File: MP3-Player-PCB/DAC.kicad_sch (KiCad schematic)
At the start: 2 parts, among them J501 AudioJack3, U501 TAD5242

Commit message: Started power schematic
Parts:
- renumbered J501 to J401, U501 to U401
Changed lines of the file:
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@@
 		(dnp no)
 		(fields_autoplaced yes)
-		(property "Reference" "J501"
+		(property "Reference" "J401"
 			(at 135.255 58.42 0)
 			(effects
@@
 			(project ""
 				(path "/3f51ea9b-d2e1-4711-a47c-269e1b97e0f4/55939feb-9632-43ca-a0aa-b7cf8cf1876d"
-					(reference "J501")
+					(reference "J401")
 					(unit 1)
 				)
@@
 		(dnp no)
 		(fields_autoplaced yes)
-		(property "Reference" "U501"
+		(property "Reference" "U401"
 			(at 96.1233 50.8 0)
 			(effects
@@
 			(project ""
 				(path "/3f51ea9b-d2e1-4711-a47c-269e1b97e0f4/55939feb-9632-43ca-a0aa-b7cf8cf1876d"
-					(reference "U501")
+					(reference "U401")
 					(unit 1)
 				)

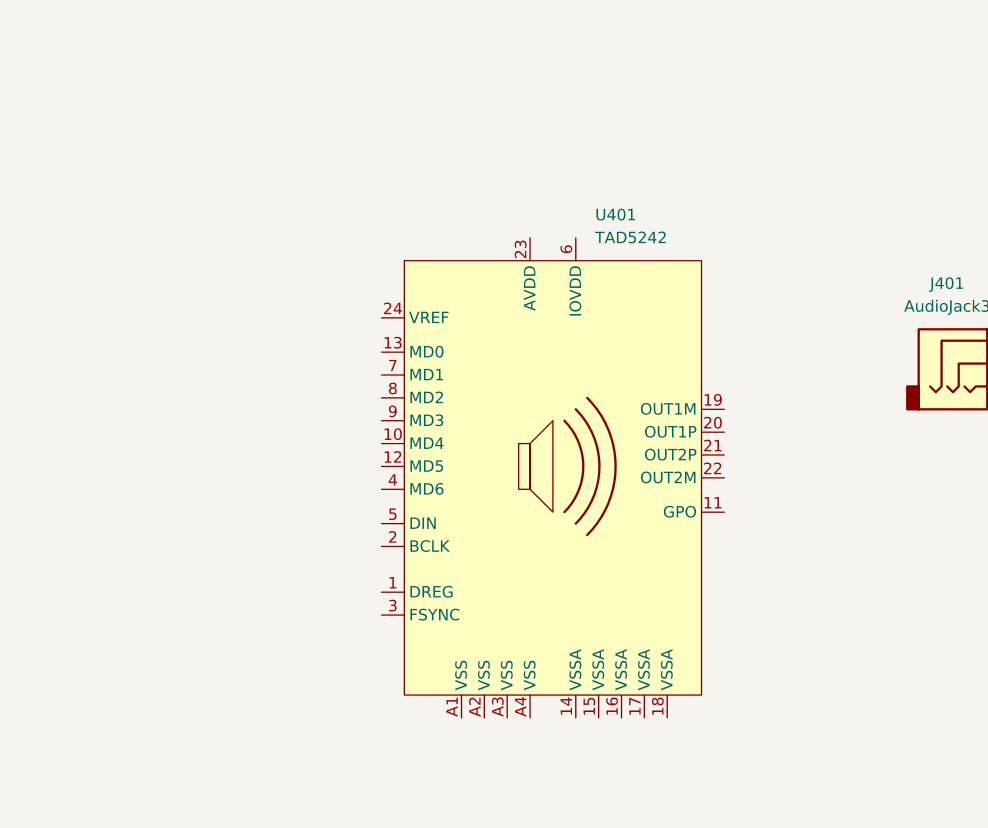
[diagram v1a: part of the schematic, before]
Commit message: Completed DAC circuitry
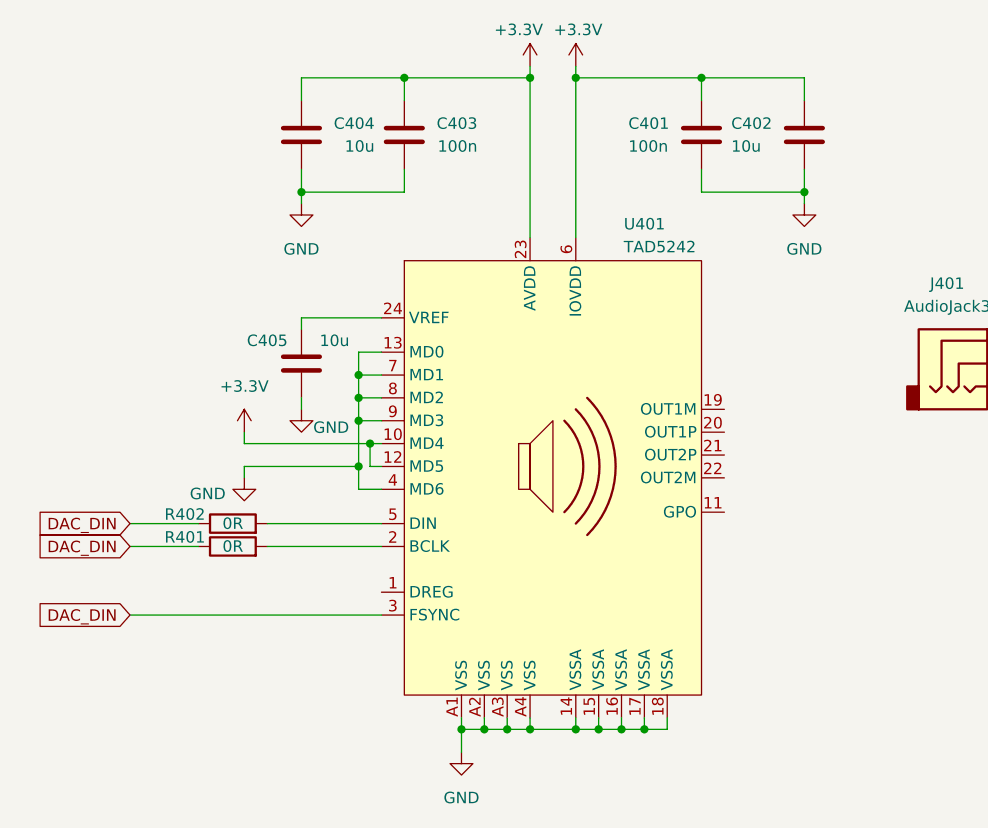
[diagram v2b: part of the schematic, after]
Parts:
- added C401, C403: 100n, symbol Device:C
- added C402, C404, C405: 10u, symbol Device:C
- added R401, R402: 0R, symbol Device:R
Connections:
- net +3.3V: now reaches U401.10 (MD4)
- net +3.3V: now also U401.12 (MD5), U401.23 (AVDD), U401.6 (IOVDD), C401.1, C402.1, C403.1, C404.1
- net GND: now reaches U401.13 (MD0)
- net GND: now also U401.14 (VSSA), U401.15 (VSSA), U401.16 (VSSA), U401.17 (VSSA), U401.18 (VSSA), U401.4 (MD6), U401.7 (MD1), U401.8 (MD2), U401.9 (MD3), U401.A1 (VSS), U401.A2 (VSS), U401.A3 (VSS), U401.A4 (VSS), C401.2, C402.2, C403.2, C404.2, C405.2
- net at U401.2 (BCLK): now also R401.2
- net at U401.24 (VREF): now also C405.1
- net DAC_DIN: now reaches U401.3 (FSYNC)
- net DAC_DIN: now also R401.1, R402.1
- net at U401.5 (DIN): now also R402.2

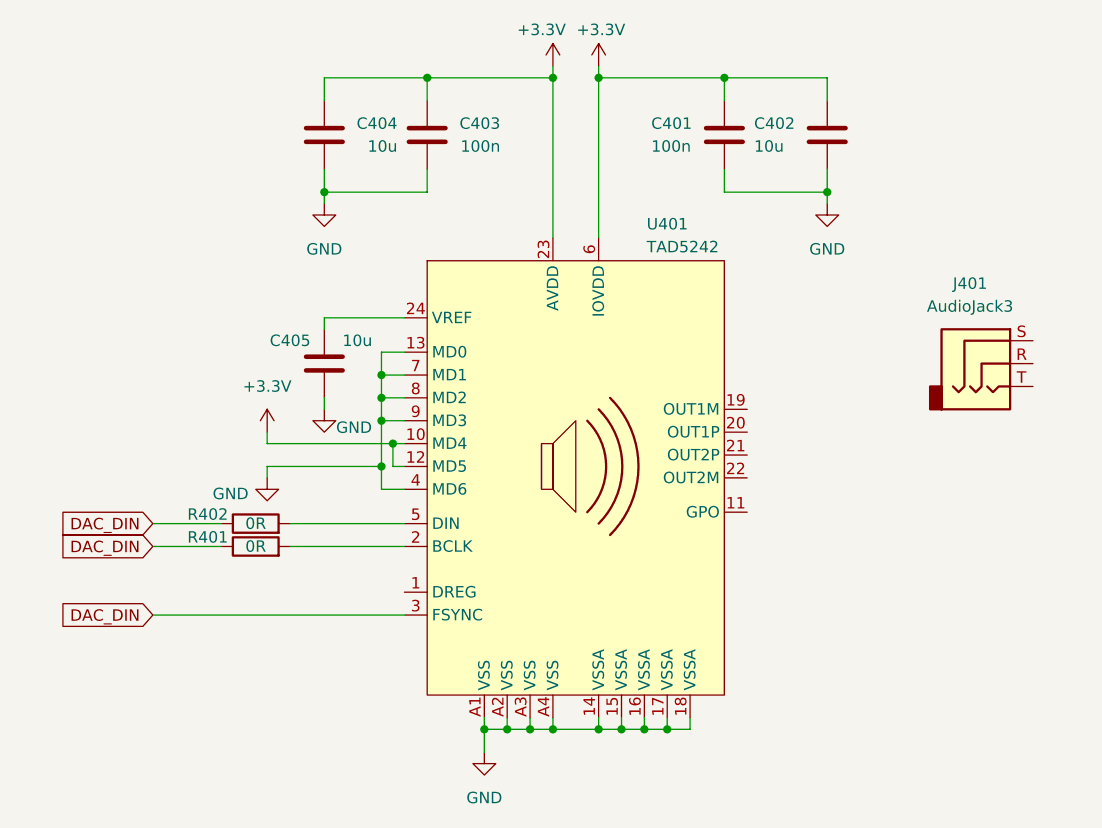
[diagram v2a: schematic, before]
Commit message: Finished SD card connections with MCU
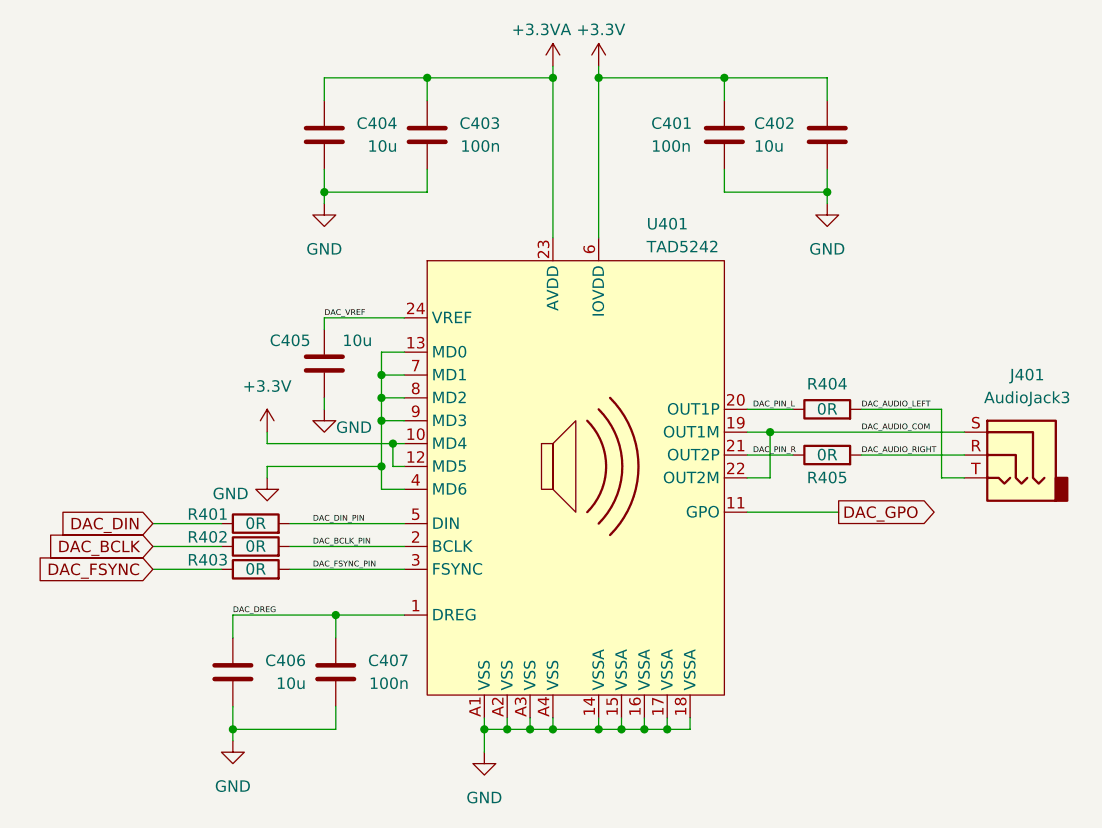
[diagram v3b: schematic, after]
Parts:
- added C406: 10u, symbol Device:C
- added C407: 100n, symbol Device:C
- added R403, R404, R405: 0R, symbol Device:R
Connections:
- net +3.3V: no longer C403.1, C404.1, U401.23 (AVDD)
- net DAC_DIN: no longer R402.1, U401.3 (FSYNC)
- net GND: now also C406.2, C407.2
- net DAC_AUDIO_RIGHT: now reaches J401.R
- net DAC_AUDIO_RIGHT: now also R405.2
- net DAC_AUDIO_COM: now reaches J401.S
- net DAC_AUDIO_COM: now also U401.19 (OUT1M), U401.22 (OUT2M)
- net DAC_AUDIO_LEFT: now reaches J401.T
- net DAC_AUDIO_LEFT: now also R404.2
- net DAC_DREG: now reaches U401.1 (DREG)
- net DAC_DREG: now also C406.1, C407.1
- net DAC_GPO: now reaches U401.11 (GPO)
- net DAC_BCLK_PIN: now reaches U401.2 (BCLK)
- net DAC_BCLK_PIN: now also R402.2; no longer R401.2
- net DAC_PIN_L: now reaches U401.20 (OUT1P)
- net DAC_PIN_L: now also R404.1
- net DAC_PIN_R: now reaches U401.21 (OUT2P)
- net DAC_PIN_R: now also R405.1
- net DAC_VREF: now reaches C405.1, U401.24 (VREF)
- net DAC_DIN_PIN: now reaches U401.5 (DIN)
- net DAC_DIN_PIN: now also R401.2; no longer R402.2
- new net +3.3VA: C403.1, C404.1, U401.23 (AVDD)
- new net DAC_BCLK: R402.1
- new net DAC_FSYNC: R403.1
- new net DAC_FSYNC_PIN: R403.2, U401.3 (FSYNC)
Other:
- moved on the sheet: J401, R401, R402

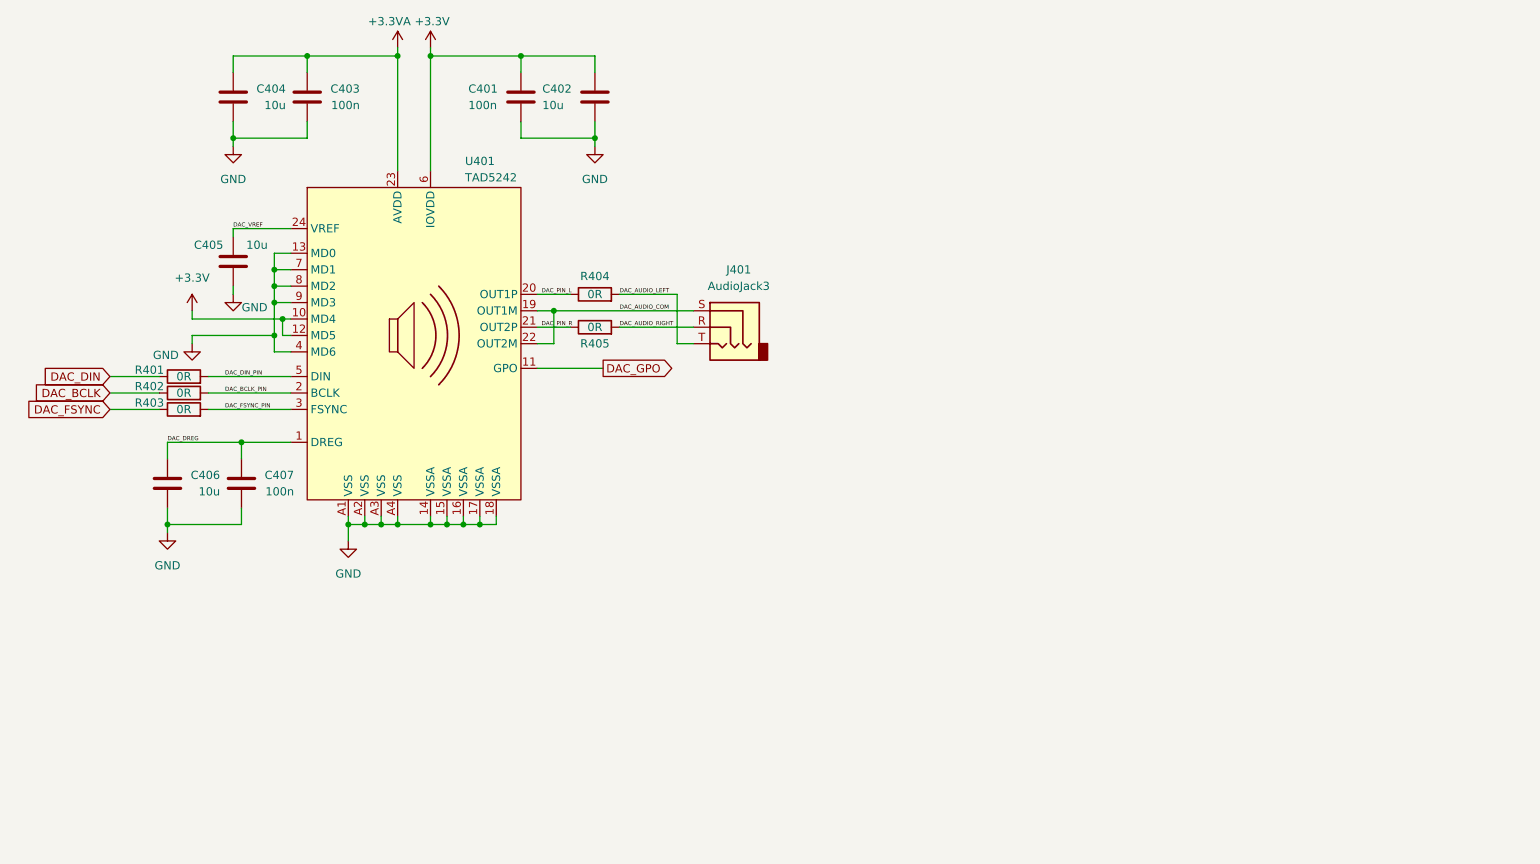
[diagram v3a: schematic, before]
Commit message: Added addressable LED circuitry
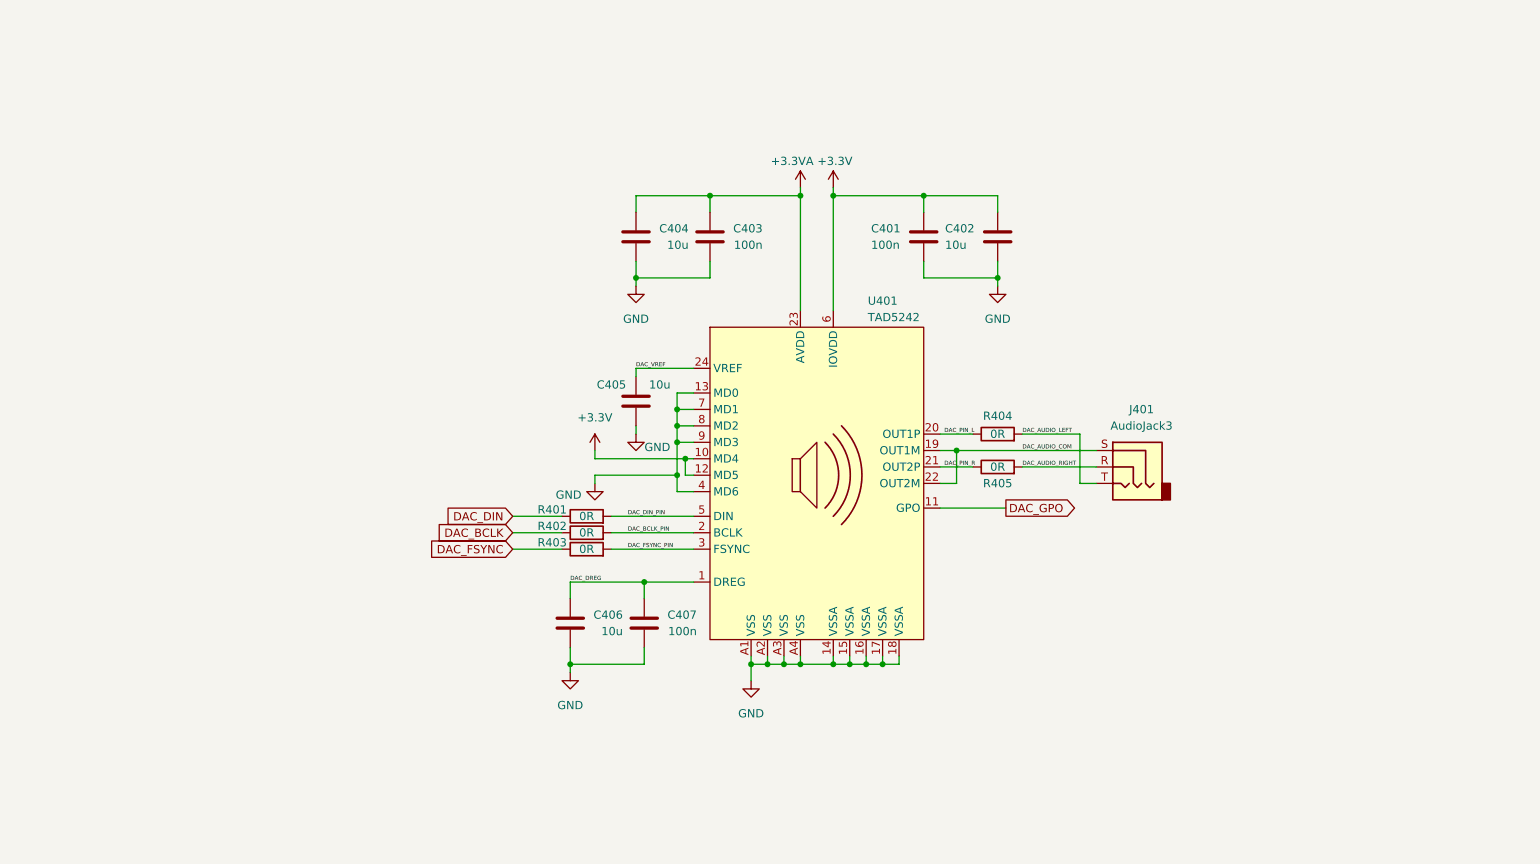
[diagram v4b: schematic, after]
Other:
- moved on the sheet: C401, C402, C403, C404, C405, C406, C407, J401, R401, R402, R403, R404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

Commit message: Added esd protection to audiojack and sd card. Also added jack detection on audiojack
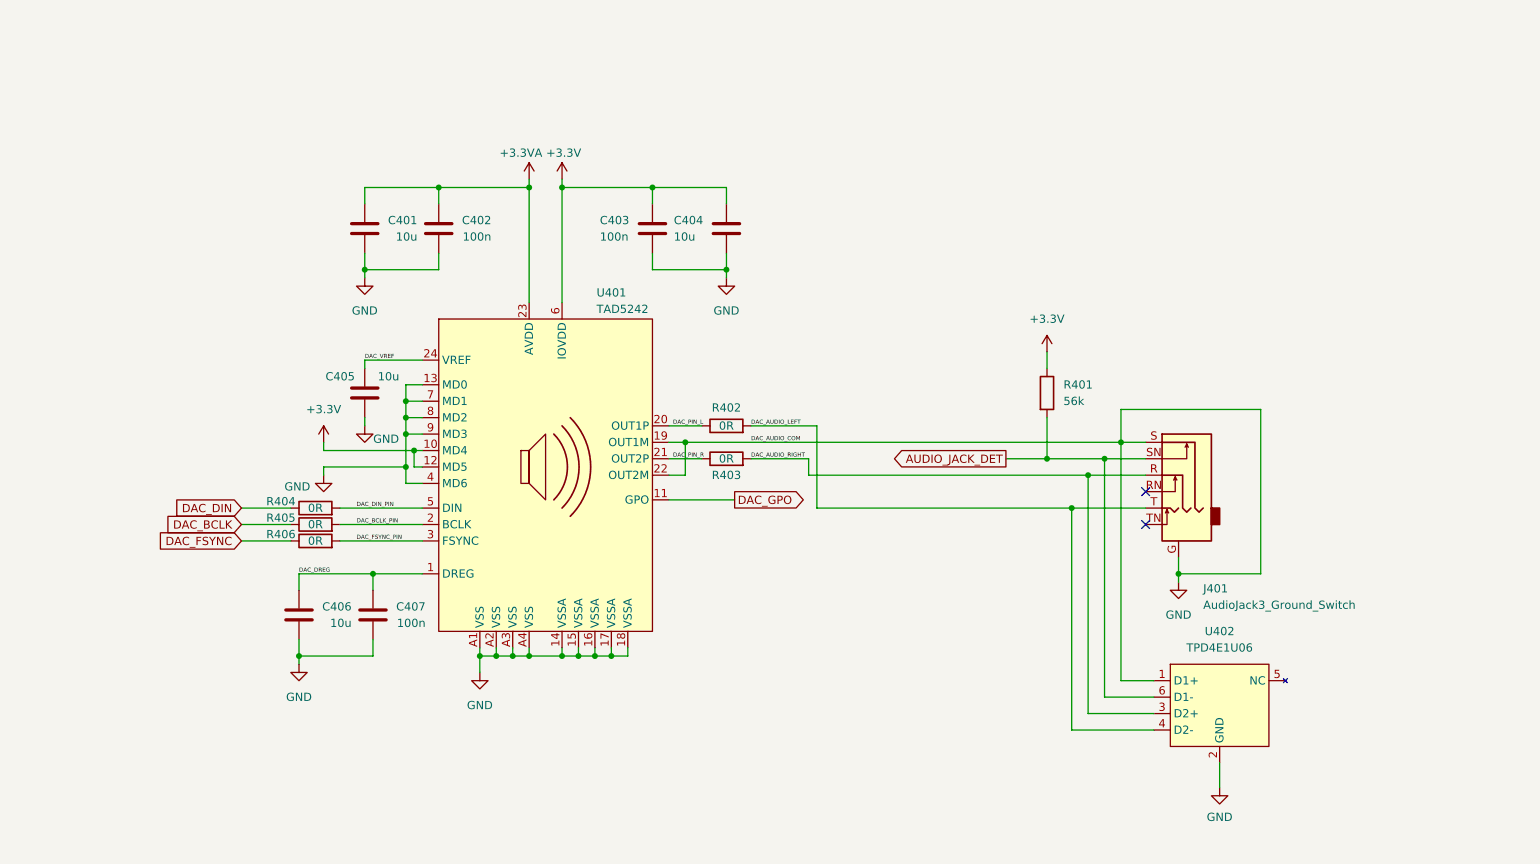
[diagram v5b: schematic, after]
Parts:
- removed J401: AudioJack3, symbol Connector_Audio:AudioJack3
- added J401: AudioJack3_Ground_Switch, symbol Connector_Audio:AudioJack3_Ground_Switch
- added R401: 56k, symbol Device:R
- added U402: TPD4E1U06, symbol MP3-Player_Symbol_Libraries:TPD4E1U06
- renumbered C404 to C401, C403 to C402, C401 to C403, C402 to C404, R404 to R402, R405 to R403, R401 to R404, R402 to R405, R403 to R406
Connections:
- net DAC_AUDIO_COM is gone; now on net GND: U401.19 (OUT1M), U401.22 (OUT2M)
- net +3.3V: now also R401.1
- net DAC_AUDIO_LEFT: now also J401.T, U402.4 (D2-)
- net DAC_AUDIO_RIGHT: now also J401.R, U402.3 (D2+)
- net GND: now also J401.G, J401.S, U402.1 (D1+), U402.2 (GND)
- new net AUDIO_JACK_DET: J401.SN, R401.2, U402.6 (D1-)
- no-connect marks 0 -> 2
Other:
- moved on the sheet: C401, C402, C403, C404, C405, C406, C407, R402, R403, R404, R405, R406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

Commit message: Added adc pin and voltage divider to read battery voltage. Also added charging status leds, and assigned some footprints
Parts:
- C401, C404, C405, C406: footprint (none) -> Capacitor_SMD:C_0805_2012Metric
- C402, C403, C407: footprint (none) -> Capacitor_SMD:C_0603_1608Metric
- U401: footprint (none) -> Package_DFN_QFN:VQFN-24-1EP_4x4mm_P0.5mm_EP2.5x2.5mm
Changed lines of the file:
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@@
 			)
 		)
-		(property "Footprint" ""
+		(property "Footprint" "Capacitor_SMD:C_0603_1608Metric"
 			(at 84.1248 125.73 0)
 			(effects
@@
 			)
 		)
-		(property "Footprint" ""
+		(property "Footprint" "Capacitor_SMD:C_0805_2012Metric"
 			(at 72.6948 125.73 0)
 			(effects
@@
 			)
 		)
-		(property "Footprint" ""
+		(property "Footprint" "Capacitor_SMD:C_0805_2012Metric"
 			(at 140.6652 66.04 0)
 			(effects
@@
 			)
 		)
-		(property "Footprint" ""
+		(property "Footprint" "Capacitor_SMD:C_0603_1608Metric"
 			(at 129.2352 66.04 0)
 			(effects
@@
 			)
 		)
-		(property "Footprint" ""
+		(property "Footprint" "Package_DFN_QFN:VQFN-24-1EP_4x4mm_P0.5mm_EP2.5x2.5mm"
 			(at 111.76 76.2 0)
 			(effects
@@
 			)
 		)
-		(property "Footprint" ""
+		(property "Footprint" "Capacitor_SMD:C_0603_1608Metric"
 			(at 94.2848 66.04 0)
 			(effects
@@
 			)
 		)
-		(property "Footprint" ""
+		(property "Footprint" "Capacitor_SMD:C_0805_2012Metric"
 			(at 82.8548 91.44 0)
 			(effects
@@
 			)
 		)
-		(property "Footprint" ""
+		(property "Footprint" "Capacitor_SMD:C_0805_2012Metric"
 			(at 82.8548 66.04 0)
 			(effects

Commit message: Assigned all footprints
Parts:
- removed J401: AudioJack3_Ground_Switch, symbol Connector_Audio:AudioJack3_Ground_Switch
- removed R401: 56k, symbol Device:R
- added R407: 56k, Resistor_SMD:R_0402_1005Metric, symbol Device:R
- added U403: ST-0322D00-071-1A2H, MP3-Player_Footprint_Libraries:ST-0322D00-071-1A2H, symbol MP3-Player_Symbol_Libraries:ST-0322D00-071-1A2H
- R402, R403, R404, R405, R406: footprint (none) -> Resistor_SMD:R_0603_1608Metric
- U402: footprint (none) -> Package_TO_SOT_SMD:SOT-23-5
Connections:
- net +3.3V: now also R407.1
- net AUDIO_JACK_DET: now also U402.1 (D1+), R407.2, U403.7 (SWITCH_1); no longer U402.6 (D1-)
- net DAC_AUDIO_LEFT: now also U403.4 (AUDIO_L)
- net DAC_AUDIO_RIGHT: now also U402.6 (D1-), U403.3 (AUDIO_R); no longer U402.3 (D2+)
- net GND: now also U402.3 (D2+), U403.1 (GND), U403.2 (MIC); no longer U402.1 (D1+)
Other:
- moved on the sheet: U402
